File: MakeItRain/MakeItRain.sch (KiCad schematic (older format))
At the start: 24 parts, among them IC1 OPA2340PA, IC2 LM2597MX-5.0_NOPB, J1 Conn_02x12_Odd_Even, J2 Conn_02x19_Odd_Even, J3 Conn_01x19, P1 Screw_Terminal_01x02, Q1 IRF9Z34NPBF, U1 178.6165.0001

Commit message: Routing Done need to add some more documentation to the board via silkscreen.
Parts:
- removed J1: Conn_02x12_Odd_Even, Connector_PinHeader_2.54mm:PinHeader_2x12_P2.54mm_Vertical, symbol Connector_Generic:Conn_02x12_Odd_Even
- added J1: Conn_02x16_Odd_Even, Connector_PinSocket_2.54mm:PinSocket_2x16_P2.54mm_Vertical, symbol Connector_Generic:Conn_02x16_Odd_Even
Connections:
- net +3V3: now also J1.2 (Pin_2)
- net +VDC: now also J1.1 (Pin_1), J1.11 (Pin_11), J1.3 (Pin_3), J1.5 (Pin_5), J1.7 (Pin_7), J1.9 (Pin_9)
- net D0: now also J1.24 (Pin_24)
- net D15: now also J1.26 (Pin_26)
- net D16: now also J1.20 (Pin_20)
- net D17: now also J1.13 (Pin_13)
- net D18: now also J1.18 (Pin_18)
- net D19: now also J1.14 (Pin_14)
- net D21: now also J1.10 (Pin_10)
- net D22: now also J1.6 (Pin_6)
- net D23: now also J1.30 (Pin_30)
- net D25: now also J1.12 (Pin_12)
- net D26: now also J1.16 (Pin_16)
- net D32: now also J1.4 (Pin_4)
- net D33: now also J1.8 (Pin_8)
- net D4: now also J1.22 (Pin_22)
- net D5: now also J1.28 (Pin_28)
- net GND: now also J1.19 (Pin_19), J1.21 (Pin_21), J1.23 (Pin_23), J1.25 (Pin_25), J1.27 (Pin_27), J1.29 (Pin_29), J1.31 (Pin_31)
- net P2: now also J1.32 (Pin_32)
- net RX: now also J1.15 (Pin_15)
- net TX: now also J1.17 (Pin_17)
- no-connect marks 14 -> 9
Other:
- moved on the sheet: R2
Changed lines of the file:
@@
 	8600 5700 8500 5700
-Wire Wire Line
-	8500 5600 8600 5600
-Wire Wire Line
-	8500 5400 8600 5400
-Wire Wire Line
-	8500 4500 8600 4500
-Wire Wire Line
-	8600 4400 8500 4400
 Wire Wire Line
 	7300 5500 7500 5500
@@
 Entry Wire Line
 	9550 4800 9650 4900
-NoConn ~ 8600 4400
-NoConn ~ 8600 4500
 NoConn ~ 8600 5800
 NoConn ~ 8600 5700
@@
 Wire Wire Line
 	8500 4100 8850 4100
-NoConn ~ 8600 5600
 $Comp
 L power:+3.3V #PWR018
@@
 	8500 5000 9550 5000
 Wire Wire Line
-	9600 5350 10150 5350
-Wire Wire Line
-	10150 3750 10150 5350
+	10150 3750 10150 5300
 Wire Bus Line
 	4650 7400 6850 7400
 Entry Wire Line
-	4550 6900 4650 7000
-Text Label 4350 6900 0    50   ~ 0
+	4550 7300 4650 7400
+Text Label 4350 7300 0    50   ~ 0
 P2
+Text Label 4350 6200 0    50   ~ 0
+D21
 Text Label 4350 6400 0    50   ~ 0
-D21
+D19
 Text Label 4350 6600 0    50   ~ 0
-D19
-Text Label 4350 6800 0    50   ~ 0
 D18
-Text Label 4350 6200 0    50   ~ 0
+Text Label 4350 6000 0    50   ~ 0
 D22
+Text Label 4350 5900 0    50   ~ 0
+D32
 Text Label 4350 6100 0    50   ~ 0
-D32
+D33
 Text Label 4350 6300 0    50   ~ 0
-D33
+D25
 Text Label 4350 6500 0    50   ~ 0
-D25
-Text Label 4350 6700 0    50   ~ 0
 D26
 Entry Wire Line
-	4550 6700 4650 6800
-Entry Wire Line
-	4550 6600 4650 6700
-Entry Wire Line
 	4550 6500 4650 6600
 Entry Wire Line
@@
 Entry Wire Line
 	4550 6100 4650 6200
-Wire Wire Line
-	3900 6800 4550 6800
-Wire Wire Line
-	4550 6700 3900 6700
+Entry Wire Line
+	4550 6000 4650 6100
+Entry Wire Line
+	4550 5900 4650 6000
 Wire Wire Line
 	3900 6600 4550 6600
@@
 	4550 6300 3900 6300
 Wire Wire Line
-	4550 6200 3900 6200
-Wire Wire Line
-	3900 6100 4550 6100
+	3900 6200 4550 6200
+Wire Wire Line
+	4550 6100 3900 6100
+Wire Wire Line
+	4550 6000 3900 6000
+Wire Wire Line
+	3900 5900 4550 5900
 $Comp
 L power:GND #PWR?
@@
 L power:+VDC #PWR?
 U 1 1 6161373B
-P 3400 5500
+P 3400 5650
 AR Path="/6158F2C4/6161373B" Ref="#PWR?"  Part="1"
 AR Path="/6161373B" Ref="#PWR07"  Part="1"
-F 0 "#PWR07" H 3400 5400 50  0001 C CNN
-F 1 "+VDC" H 3400 5775 50  0000 C CNN
-F 2 "" H 3400 5500 50  0001 C CNN
-F 3 "" H 3400 5500 50  0001 C CNN
-	1    3400 5500
-	1    0    0    -1
-$EndComp
-Wire Wire Line
-	4550 6900 4100 6900
+F 0 "#PWR07" H 3400 5550 50  0001 C CNN
+F 1 "+VDC" H 3400 5925 50  0000 C CNN
+F 2 "" H 3400 5650 50  0001 C CNN
+F 3 "" H 3400 5650 50  0001 C CNN
+	1    3400 5650
+	1    0    0    -1
+$EndComp
+Wire Wire Line
+	4550 7300 4100 7300
 $Comp
 L power:+3.3V #PWR010
 U 1 1 6190DF70
-P 3900 5450
-F 0 "#PWR010" H 3900 5300 50  0001 C CNN
-F 1 "+3.3V" H 3915 5623 50  0000 C CNN
-F 2 "" H 3900 5450 50  0001 C CNN
-F 3 "" H 3900 5450 50  0001 C CNN
-	1    3900 5450
+P 3900 5650
+F 0 "#PWR010" H 3900 5500 50  0001 C CNN
+F 1 "+3.3V" H 3915 5823 50  0000 C CNN
+F 2 "" H 3900 5650 50  0001 C CNN
+F 3 "" H 3900 5650 50  0001 C CNN
+	1    3900 5650
 	1    0    0    -1
 $EndComp
@@
 L Device:R R?
 U 1 1 619FD932
-P 4100 7100
+P 4100 7500
 AR Path="/6158F2C4/619FD932" Ref="R?"  Part="1"
 AR Path="/619FD932" Ref="R2"  Part="1"
-F 0 "R2" H 4170 7146 50  0000 L CNN
-F 1 "22k" H 4170 7055 50  0000 L CNN
-F 2 "Resistor_THT:R_Axial_DIN0207_L6.3mm_D2.5mm_P5.08mm_Vertical" V 4030 7100 50  0001 C CNN
-F 3 "~" H 4100 7100 50  0001 C CNN
-	1    4100 7100
+F 0 "R2" H 4170 7546 50  0000 L CNN
+F 1 "22k" H 4170 7455 50  0000 L CNN
+F 2 "Resistor_THT:R_Axial_DIN0207_L6.3mm_D2.5mm_P5.08mm_Vertical" V 4030 7500 50  0001 C CNN
+F 3 "~" H 4100 7500 50  0001 C CNN
+	1    4100 7500
 	1    0    0    -1
 $EndComp
@@
 L power:GND #PWR?
 U 1 1 619FD938
-P 4100 7300
+P 4100 7700
 AR Path="/6158F2C4/619FD938" Ref="#PWR?"  Part="1"
 AR Path="/619FD938" Ref="#PWR011"  Part="1"
-F 0 "#PWR011" H 4100 7050 50  0001 C CNN
-F 1 "GND" H 4105 7127 50  0000 C CNN
-F 2 "" H 4100 7300 50  0001 C CNN
-F 3 "" H 4100 7300 50  0001 C CNN
-	1    4100 7300
-	1    0    0    -1
-$EndComp
-Wire Wire Line
-	4100 7250 4100 7300
-Wire Wire Line
-	4100 6950 4100 6900
-Connection ~ 4100 6900
-Wire Wire Line
-	4100 6900 3900 6900
-NoConn ~ 8600 5400
+F 0 "#PWR011" H 4100 7450 50  0001 C CNN
+F 1 "GND" H 4105 7527 50  0000 C CNN
+F 2 "" H 4100 7700 50  0001 C CNN
+F 3 "" H 4100 7700 50  0001 C CNN
+	1    4100 7700
+	1    0    0    -1
+$EndComp
+Wire Wire Line
+	4100 7650 4100 7700
+Wire Wire Line
+	4100 7350 4100 7300
+Connection ~ 4100 7300
+Wire Wire Line
+	4100 7300 3900 7300
+Text Label 4700 6050 0    50   ~ 0
+Z5
 Text Label 4700 6250 0    50   ~ 0
-Z5
+Z6
 Text Label 4700 6450 0    50   ~ 0
-Z6
+Z7
 Text Label 4700 6650 0    50   ~ 0
-Z7
-Text Label 4700 6850 0    50   ~ 0
 Z8
-Text Label 4100 7300 0    50   ~ 0
+Text Label 4100 7700 0    50   ~ 0
 BoardSense
 Text Label 8600 5200 0    50   ~ 0
@@
 Text Label 8600 5300 0    50   ~ 0
 D4
-Wire Wire Line
-	8500 5300 9600 5300
-Wire Wire Line
-	9600 5300 9600 5350
-Wire Wire Line
-	8500 5200 8600 5200
 Entry Wire Line
 	9550 5500 9650 5600
 Wire Wire Line
 	8500 5500 9550 5500
-NoConn ~ 8600 5200
+Entry Wire Line
+	4550 6600 4650 6700
+Entry Wire Line
+	9550 5600 9650 5700
+Wire Wire Line
+	8500 5600 9550 5600
+Entry Wire Line
+	9550 5400 9650 5500
+Wire Wire Line
+	8500 5400 9550 5400
+Entry Wire Line
+	9550 5200 9650 5300
+Wire Wire Line
+	8500 5200 9550 5200
+Entry Wire Line
+	9550 4500 9650 4600
+Wire Wire Line
+	8500 4500 9550 4500
+Entry Wire Line
+	9550 4400 9650 4500
+Wire Wire Line
+	8500 4400 9550 4400
+Text Label 4350 7200 0    50   ~ 0
+D23
+Text Label 4350 7000 0    50   ~ 0
+D15
+Text Label 4400 5350 0    50   ~ 0
+D17
+Text Label 4450 7100 0    50   ~ 0
+D5
+Text Label 4400 5250 0    50   ~ 0
+RX
+Text Label 4400 5150 0    50   ~ 0
+TX
+Text Label 4400 6700 0    50   ~ 0
+D16
+Text Label 4400 6800 0    50   ~ 0
+D4
+Wire Wire Line
+	3900 6900 4550 6900
+Entry Wire Line
+	4550 6900 4650 7000
+Wire Wire Line
+	3900 6700 4550 6700
+Entry Wire Line
+	4550 6700 4650 6800
+Entry Wire Line
+	4550 5150 4650 5250
+Wire Wire Line
+	3900 6800 4550 6800
 Entry Wire Line
 	4550 6800 4650 6900
-$Comp
-L Connector_Generic:Conn_02x12_Odd_Even J1
-U 1 1 6164B72D
-P 3600 6300
-F 0 "J1" H 3650 7017 50  0000 C CNN
-F 1 "Conn_02x12_Odd_Even" H 3650 6926 50  0000 C CNN
-F 2 "Connector_PinHeader_2.54mm:PinHeader_2x12_P2.54mm_Vertical" H 3600 6300 50  0001 C CNN
-F 3 "~" H 3600 6300 50  0001 C CNN
-	1    3600 6300
-	1    0    0    -1
-$EndComp
-Wire Wire Line
-	3900 5450 3900 5800
-Wire Wire Line
-	3400 5500 3400 5800
-Wire Wire Line
-	3900 5900 3900 6000
-Wire Wire Line
-	3400 6900 3400 7400
+Text Label 4400 6900 0    50   ~ 0
+D0
+Wire Wire Line
+	3900 7100 4550 7100
+Entry Wire Line
+	4550 7100 4650 7200
+Entry Wire Line
+	4550 5350 4650 5450
+Entry Wire Line
+	4550 5250 4650 5350
+Wire Wire Line
+	3900 7000 4550 7000
+Entry Wire Line
+	4550 7000 4650 7100
+Entry Wire Line
+	4550 7200 4650 7300
+Wire Wire Line
+	3900 7200 4550 7200
+$Comp
+L Connector_Generic:Conn_02x16_Odd_Even J1
+U 1 1 617F2752
+P 3600 6500
+F 0 "J1" H 3650 7417 50  0000 C CNN
+F 1 "Conn_02x16_Odd_Even" H 3650 7326 50  0000 C CNN
+F 2 "Connector_PinSocket_2.54mm:PinSocket_2x16_P2.54mm_Vertical" H 3600 6500 50  0001 C CNN
+F 3 "~" H 3600 6500 50  0001 C CNN
+	1    3600 6500
+	1    0    0    -1
+$EndComp
 Wire Wire Line
 	3400 5800 3400 5900
@@
 Connection ~ 3400 6100
 Wire Wire Line
+	3400 7400 3400 7300
+Wire Wire Line
+	3400 7300 3400 7200
+Connection ~ 3400 7300
+Wire Wire Line
+	3400 7200 3400 7100
+Connection ~ 3400 7200
+Wire Wire Line
+	3400 7100 3400 7000
+Connection ~ 3400 7100
+Wire Wire Line
+	3400 7000 3400 6900
+Connection ~ 3400 7000
+Wire Wire Line
+	3900 5650 3900 5800
+Wire Wire Line
+	3400 5650 3400 5800
+Wire Wire Line
+	3000 5350 3000 6400
+Wire Wire Line
+	3000 6400 3400 6400
+Wire Wire Line
+	3000 5350 4550 5350
+Wire Wire Line
+	2950 5250 2950 6500
+Wire Wire Line
+	2950 6500 3400 6500
+Wire Wire Line
+	2950 5250 4550 5250
+Wire Wire Line
+	3400 6600 2900 6600
+Wire Wire Line
+	2900 6600 2900 5150
+Wire Wire Line
+	2900 5150 4550 5150
+Wire Wire Line
+	3400 6300 3400 6200
+Connection ~ 3400 6200
+Wire Wire Line
 	3400 6900 3400 6800
 Connection ~ 3400 6900
@@
 Connection ~ 3400 6800
 Wire Wire Line
-	3400 6700 3400 6600
-Connection ~ 3400 6700
-Wire Wire Line
-	3400 6600 3400 6500
-Connection ~ 3400 6600
-Wire Wire Line
-	3400 6500 3400 6400
-Connection ~ 3400 6500
-Wire Wire Line
-	3400 6300 3400 6200
-Connection ~ 3400 6200
+	8500 5300 10150 5300
+Wire Bus Line
+	6850 4400 6850 6450
 Wire Bus Line
 	9650 4300 9650 6450
 Wire Bus Line
-	6850 4400 6850 6450
-Wire Bus Line
 	4650 3200 4650 7400

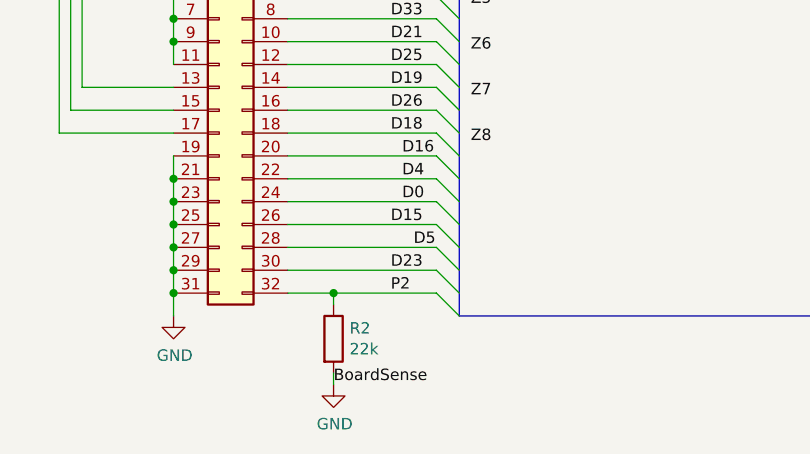
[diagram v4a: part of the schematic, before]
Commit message: Fixed a few fuck up on the board and schematic. a label wasn't correct and thus wasn't routed. Changed the VDC power to the zones from a 40mil trace to a plane. added silkscreen stuff to the board.
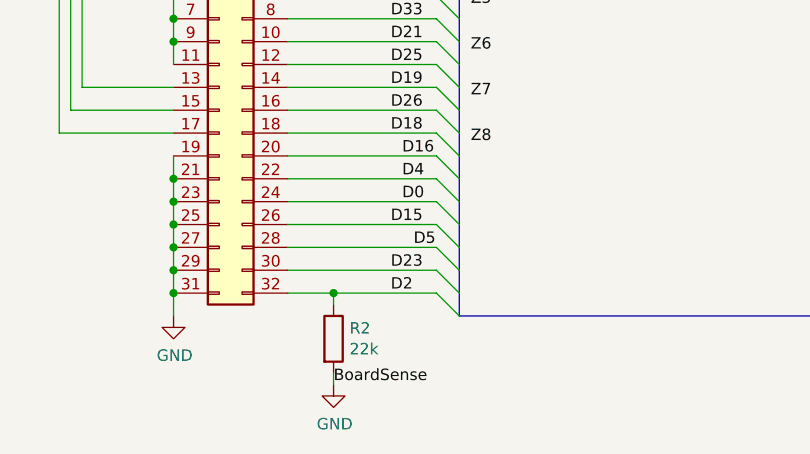
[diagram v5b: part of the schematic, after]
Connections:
- net P2 is gone; now on net D2: J1.32 (Pin_32), R2.1
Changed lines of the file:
@@
 Connection ~ 7500 5600
-Wire Wire Line
-	8000 5700 7500 5700
-Connection ~ 7500 5700
 Wire Wire Line
 	8000 5800 7500 5800
@@
 	4550 7300 4650 7400
 Text Label 4350 7300 0    50   ~ 0
-P2
+D2
 Text Label 4350 6200 0    50   ~ 0
 D21
@@
 Wire Bus Line
 	4650 3200 4650 7400
+Connection ~ 7500 5700
+Wire Wire Line
+	8000 5700 7500 5700
 $EndSCHEMATC

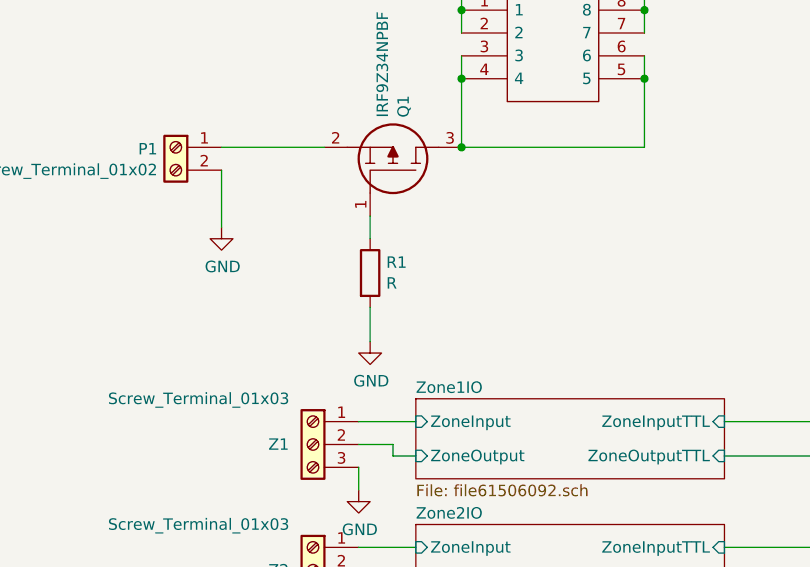
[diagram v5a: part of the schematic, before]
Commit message: updated resistor values on the boards that weren't defined.
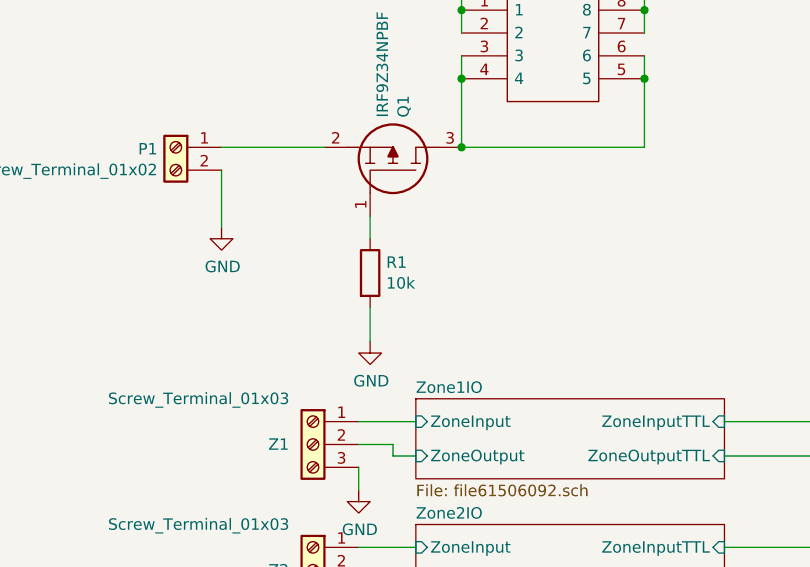
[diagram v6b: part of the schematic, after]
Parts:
- R1: value R -> 10k
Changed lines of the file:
@@
 AR Path="/614DBB1F" Ref="R1"  Part="1"
 F 0 "R1" H 2420 2496 50  0000 L CNN
-F 1 "R" H 2420 2405 50  0000 L CNN
+F 1 "10k" H 2420 2405 50  0000 L CNN
 F 2 "Resistor_THT:R_Axial_DIN0207_L6.3mm_D2.5mm_P5.08mm_Vertical" V 2280 2450 50  0001 C CNN
 F 3 "~" H 2350 2450 50  0001 C CNN
@@
 	3400 6800 3400 6700
 Connection ~ 3400 6800
+Connection ~ 7500 5700
+Wire Wire Line
+	8000 5700 7500 5700
 Wire Wire Line
 	8500 5300 10150 5300
@@
 Wire Bus Line
 	4650 3200 4650 7400
-Connection ~ 7500 5700
-Wire Wire Line
-	8000 5700 7500 5700
 $EndSCHEMATC

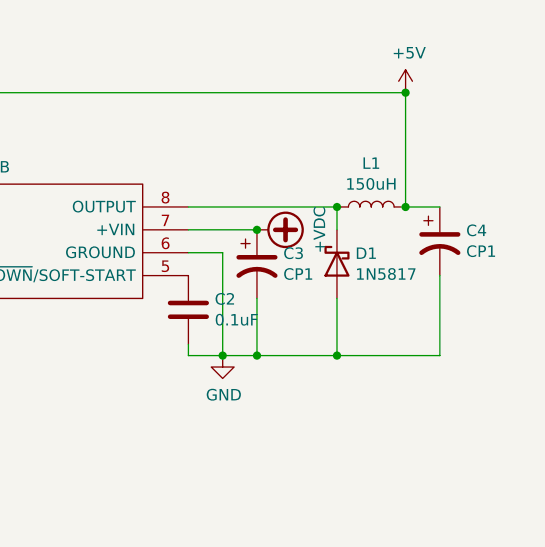
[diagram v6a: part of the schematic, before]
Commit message: updated some missing values on the schematic.
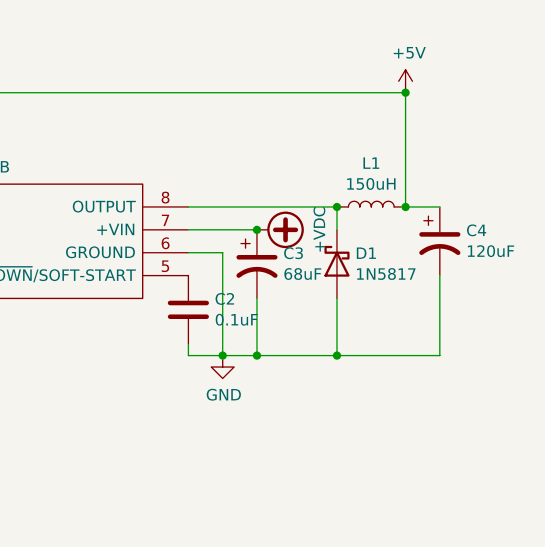
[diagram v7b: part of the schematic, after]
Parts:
- C3: value CP1 -> 68uF
- C4: value CP1 -> 120uF
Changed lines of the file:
@@
 P 10100 1650
 F 0 "C3" H 10215 1696 50  0000 L CNN
-F 1 "CP1" H 10215 1605 50  0000 L CNN
+F 1 "68uF" H 10215 1605 50  0000 L CNN
 F 2 "Capacitor_THT:CP_Radial_D8.0mm_P3.50mm" H 10100 1650 50  0001 C CNN
 F 3 "~" H 10100 1650 50  0001 C CNN
@@
 P 10900 1550
 F 0 "C4" H 11015 1596 50  0000 L CNN
-F 1 "CP1" H 11015 1505 50  0000 L CNN
+F 1 "120uF" H 11015 1505 50  0000 L CNN
 F 2 "Capacitor_THT:CP_Radial_D8.0mm_P3.50mm" H 10900 1550 50  0001 C CNN
 F 3 "~" H 10900 1550 50  0001 C CNN

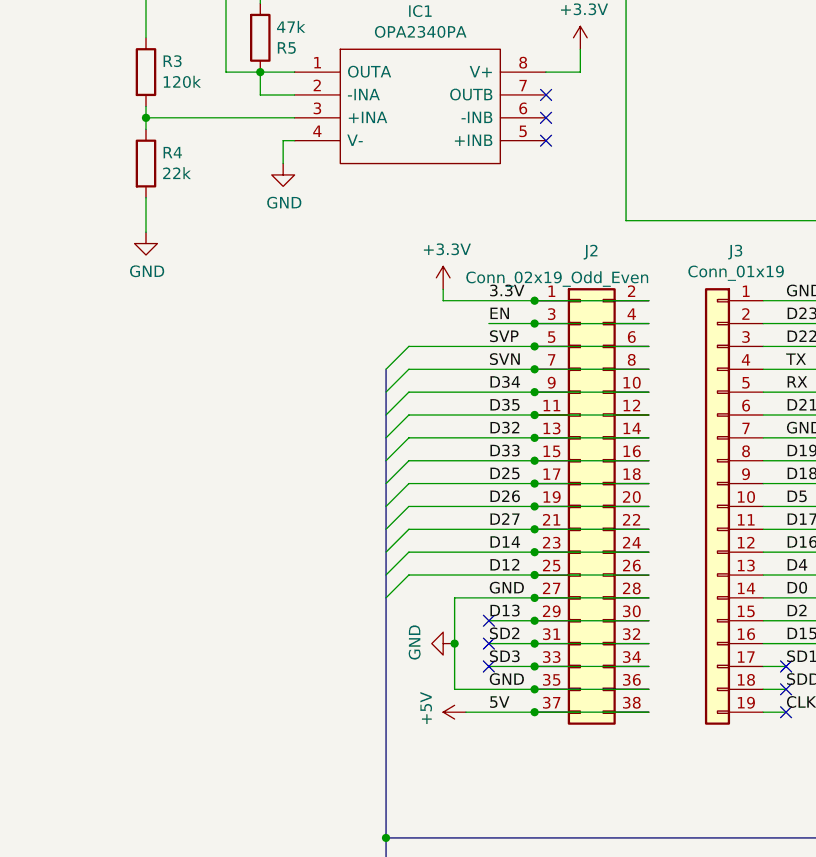
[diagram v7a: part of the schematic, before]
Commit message: updated fab files and some values on the schematic. this is to fix the problem with grounding one of the ground pins and it affecting the dev board running and being able to load.
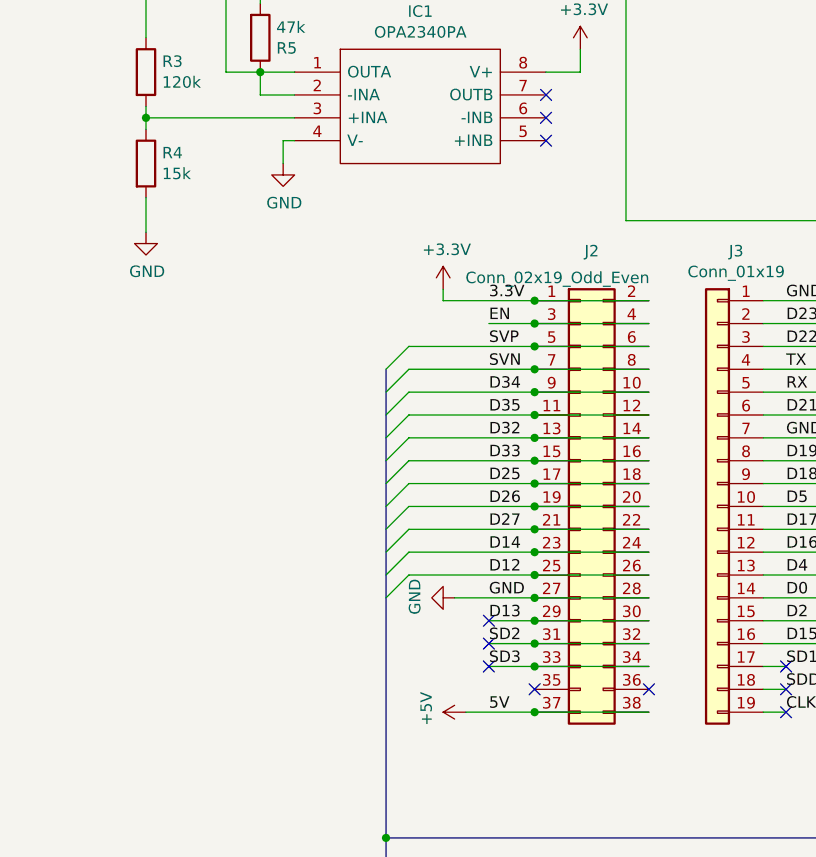
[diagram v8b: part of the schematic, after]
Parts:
- R4: value 22k -> 15k
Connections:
- net GND: no longer J2.35 (Pin_35), J2.36 (Pin_36)
- no-connect marks 9 -> 11
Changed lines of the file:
@@
 AR Path="/614FC77C" Ref="R4"  Part="1"
 F 0 "R4" H 5870 3546 50  0000 L CNN
-F 1 "22k" H 5870 3455 50  0000 L CNN
+F 1 "15k" H 5870 3455 50  0000 L CNN
 F 2 "Resistor_THT:R_Axial_DIN0207_L6.3mm_D2.5mm_P5.08mm_Vertical" V 5730 3500 50  0001 C CNN
 F 3 "~" H 5800 3500 50  0001 C CNN
@@
 Text Label 7300 5900 0    50   ~ 0
 5V
-Text Label 7300 5800 0    50   ~ 0
-GND
 Text Label 7300 5700 0    50   ~ 0
 SD3
@@
 Wire Wire Line
 	7150 5400 7500 5400
-Wire Wire Line
-	7150 5800 7500 5800
 $Comp
 L power:GND #PWR019
 U 1 1 61562C8D
-P 7150 5600
-F 0 "#PWR019" H 7150 5350 50  0001 C CNN
-F 1 "GND" H 7155 5427 50  0000 C CNN
-F 2 "" H 7150 5600 50  0001 C CNN
-F 3 "" H 7150 5600 50  0001 C CNN
-	1    7150 5600
+P 7150 5400
+F 0 "#PWR019" H 7150 5150 50  0001 C CNN
+F 1 "GND" H 7155 5227 50  0000 C CNN
+F 2 "" H 7150 5400 50  0001 C CNN
+F 3 "" H 7150 5400 50  0001 C CNN
+	1    7150 5400
 	0    1    -1   0
 $EndComp
-Wire Wire Line
-	7150 5400 7150 5600
-Wire Wire Line
-	7150 5600 7150 5800
-Connection ~ 7150 5600
 Wire Bus Line
 	6850 7400 6850 6450
@@
 	8000 5600 7500 5600
 Connection ~ 7500 5600
-Wire Wire Line
-	8000 5800 7500 5800
-Connection ~ 7500 5800
 Wire Wire Line
 	8000 5900 7500 5900
@@
 Wire Wire Line
 	8000 5700 7500 5700
+NoConn ~ 8000 5800
+NoConn ~ 7500 5800
 Wire Wire Line
 	8500 5300 10150 5300
